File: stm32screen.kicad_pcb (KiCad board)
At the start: 4 copper layers, 49.8 x 49.8 mm, 43 parts, among them J1 SWD, J2 GC9A01, J3 Oil temp sensor, J4 pressure sensor, J5 USB_B_Micro, J6 EGT_sensor, SW1 SW_Push, SW2 SW_Push, U1 TS1117BCW-3.3, U2 STM32F407VETx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

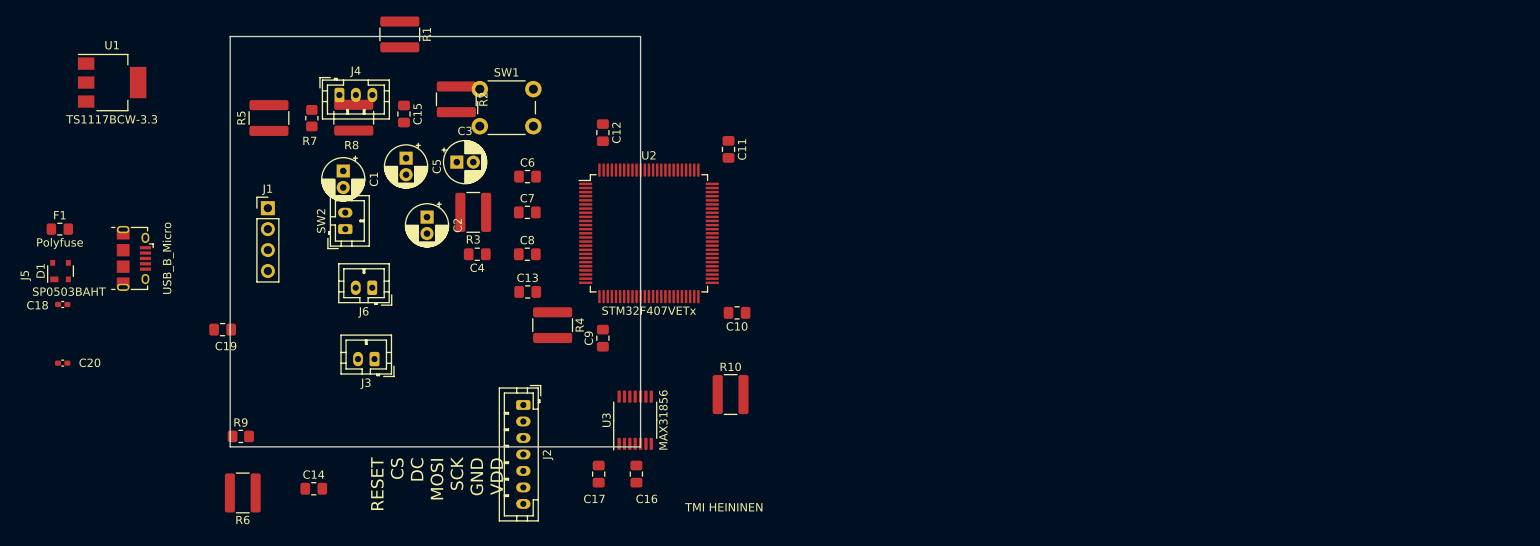
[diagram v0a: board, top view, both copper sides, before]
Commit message: Roughing out the PCB.
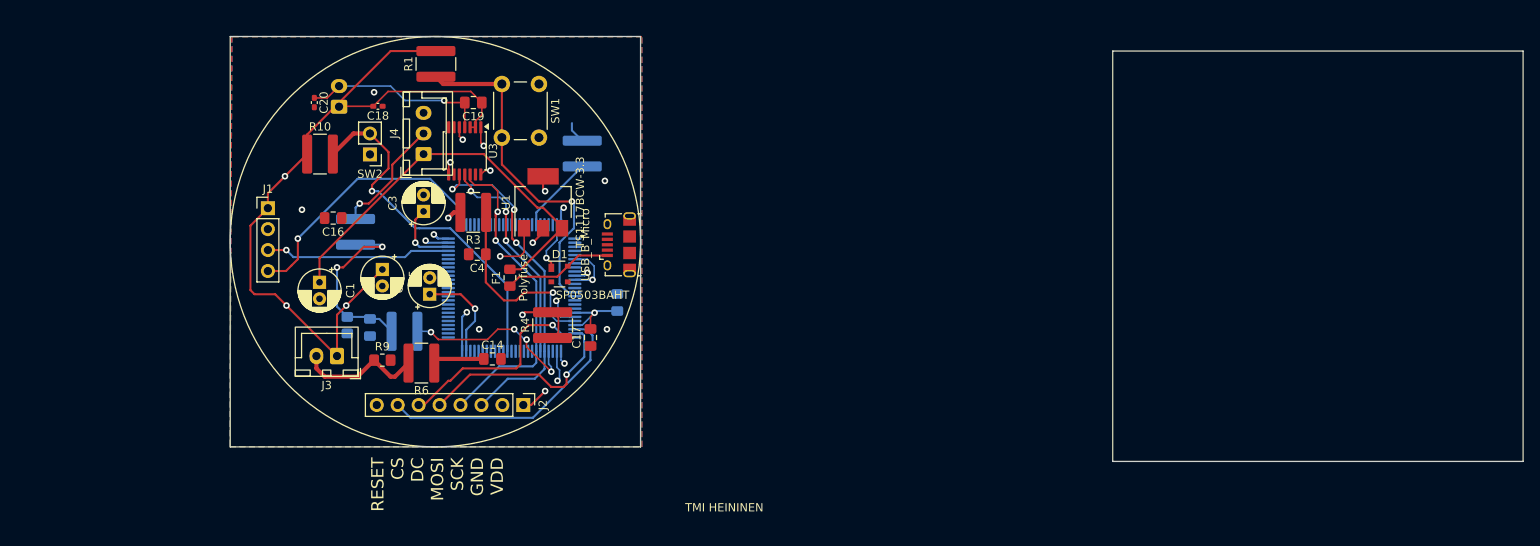
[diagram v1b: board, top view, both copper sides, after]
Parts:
- removed C10, C11, C12, C6, C7, C8, C9: 100nF, Capacitor_SMD:C_0805_2012Metric_Pad1.18x1.45mm_HandSolder
- C13, C15, R2, R5, R7, R8, U2: moved to B.Cu
- J2: footprint Connector_JST:JST_PH_B7B-PH-K_1x07_P2.00mm_Vertical -> Connector_PinHeader_2.54mm:PinHeader_1x08_P2.54mm_Vertical
- J3: footprint Connector_JST:JST_PH_B2B-PH-K_1x02_P2.00mm_Vertical -> Connector_JST:JST_XH_B2B-XH-A_1x02_P2.50mm_Vertical
- J4: footprint Connector_JST:JST_PH_B3B-PH-K_1x03_P2.00mm_Vertical -> Connector_JST:JST_XH_B3B-XH-A_1x03_P2.50mm_Vertical
- J6: footprint Connector_JST:JST_PH_B2B-PH-K_1x02_P2.00mm_Vertical -> Connector_JST:JST_XH_B2B-XH-A_1x02_P2.50mm_Vertical; moved to B.Cu
- SW2: footprint Connector_JST:JST_PH_B2B-PH-K_1x02_P2.00mm_Vertical -> Connector_PinHeader_2.54mm:PinHeader_1x02_P2.54mm_Vertical
- moved D1 60.5 mm to (138.0, 75.5), turned to 0 degrees
- moved J5 58.9 mm to (145.2, 72.0), turned to 90 degrees
- moved R10 57.7 mm to (108.9, 61.0)
- moved F1 54.9 mm to (132.0, 76.0), turned to 90 degrees
- moved U1 54.3 mm to (136.0, 66.8), turned to 90 degrees
- moved C16 48.1 mm to (110.5, 68.8), turned to 180 degrees
- moved C18 45.2 mm to (116.0, 55.2)
- moved C20 43.9 mm to (108.2, 54.8), turned to -90 degrees
- moved C19 41.0 mm to (127.5, 54.8)
- moved U3 38.7 mm to (126.5, 60.6), turned to -90 degrees
- moved R5 30.7 mm to (119.2, 82.5), turned to 180 degrees
- moved R6 26.8 mm to (121.2, 86.4)
- moved C14 26.8 mm to (129.9, 85.8)
- moved C15 26.2 mm to (115.0, 82.0)
- moved R7 25.5 mm to (112.2, 81.8)
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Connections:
- net /SCK renamed SCK
- net /SPI1_MOSI renamed SDI
- net Net-(U2-Pad31) renamed SDO
- C13 pad 2: Net-(C13-Pad2) -> VDD
- R4 pad 1: Net-(C13-Pad2) -> VDD
- U2 pad 22: Net-(C13-Pad2) -> VDD
- U2 pad 35: Net-(U2-Pad35) -> MAX_CS
- U2 pad 36: Net-(U2-Pad36) -> MAX-FAULT
- U2 pad 37: Net-(U2-Pad37) -> MAX_DRDY
- U3 pad 13: Net-(U2-Pad36) -> FAULT
- U3 pad 7: Net-(U2-Pad37) -> DRDY
- U3 pad 9: Net-(U2-Pad35) -> CS
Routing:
- net VDD: track 0.00 -> 114.6 mm, vias 0 -> 15
- net Vin: track 0.00 -> 49.8 mm
- net Net-(U2-PE8): track 0.00 -> 43.5 mm, vias 0 -> 1
- net SCK: track 0.00 -> 41.9 mm, vias 0 -> 3
- net NRST: track 0.00 -> 41.6 mm, vias 0 -> 1
- net SDI: track 0.00 -> 38.9 mm, vias 0 -> 2
- net /SWCLK: track 0.00 -> 33.0 mm, vias 0 -> 1
- net /RESET: track 0.00 -> 32.5 mm
- net GND: track 0.00 -> 30.6 mm, vias 0 -> 13
- net SDO: track 0.00 -> 26.9 mm, vias 0 -> 3
- net /CS: track 0.00 -> 25.8 mm, vias 0 -> 1
- net /D/C: track 0.00 -> 25.7 mm, vias 0 -> 1
- net Net-(U2-VREF+): track 0.00 -> 24.0 mm, vias 0 -> 1
- net Net-(J6-Pin_2): track 0.00 -> 22.7 mm, vias 0 -> 1
- net Net-(J6-Pin_1): track 0.00 -> 22.6 mm
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- added copper zone on B.Cu, net GND
- added copper zone on F.Cu, net GND
- added copper zone on In2.Cu, net GND
- added copper zone on In1.Cu, net VDD
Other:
- board size 49.8 x 49.8 mm -> 156.8 x 51.5 mm

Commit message: Routed rest of the unconnected pads
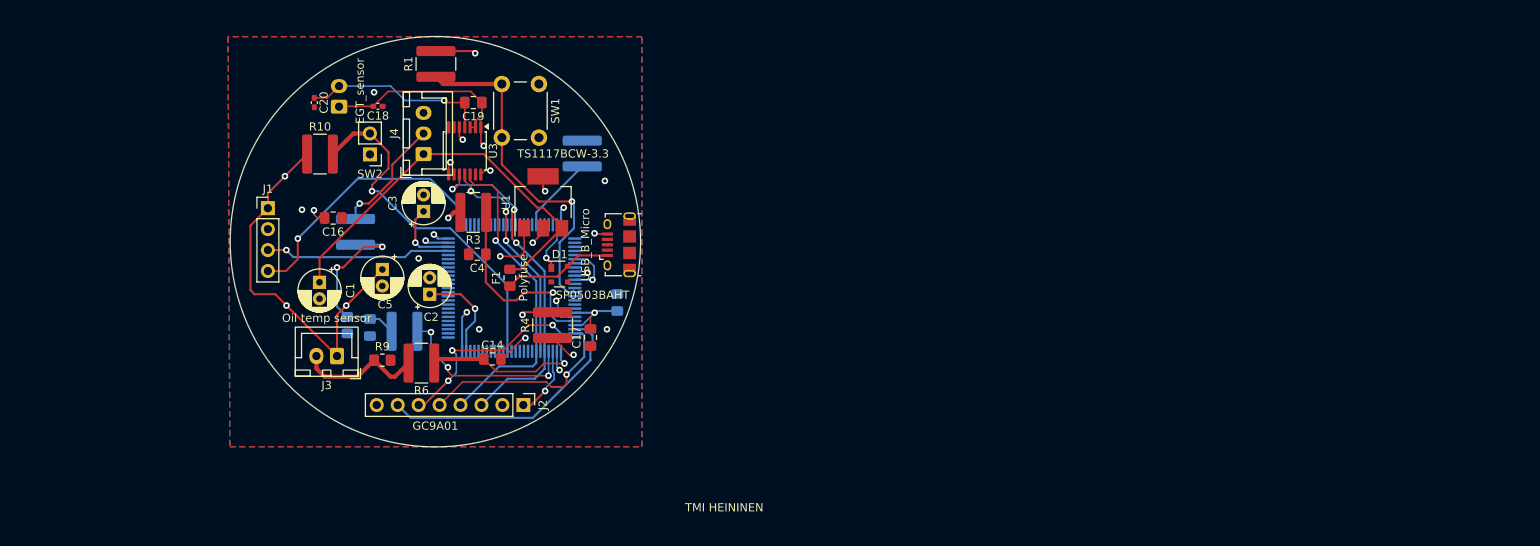
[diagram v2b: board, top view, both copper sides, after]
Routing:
- net Net-(U2-PA3): track 7.88 -> 18.7 mm
- net VDD: track 114.6 -> 104.3 mm, vias 15 -> 18
- net GND: track 30.6 -> 32.2 mm, vias 13 -> 16
- net /D/C: track 25.7 -> 25.0 mm
- net Net-(U2-PA4): track 22.5 -> 22.7 mm, vias 4 -> 3
- net /CS: track 25.8 -> 25.9 mm, vias 1 -> 3
- net SDI: vias 2 -> 1
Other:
- board size 156.8 x 51.5 mm -> 49.8 x 49.8 mm

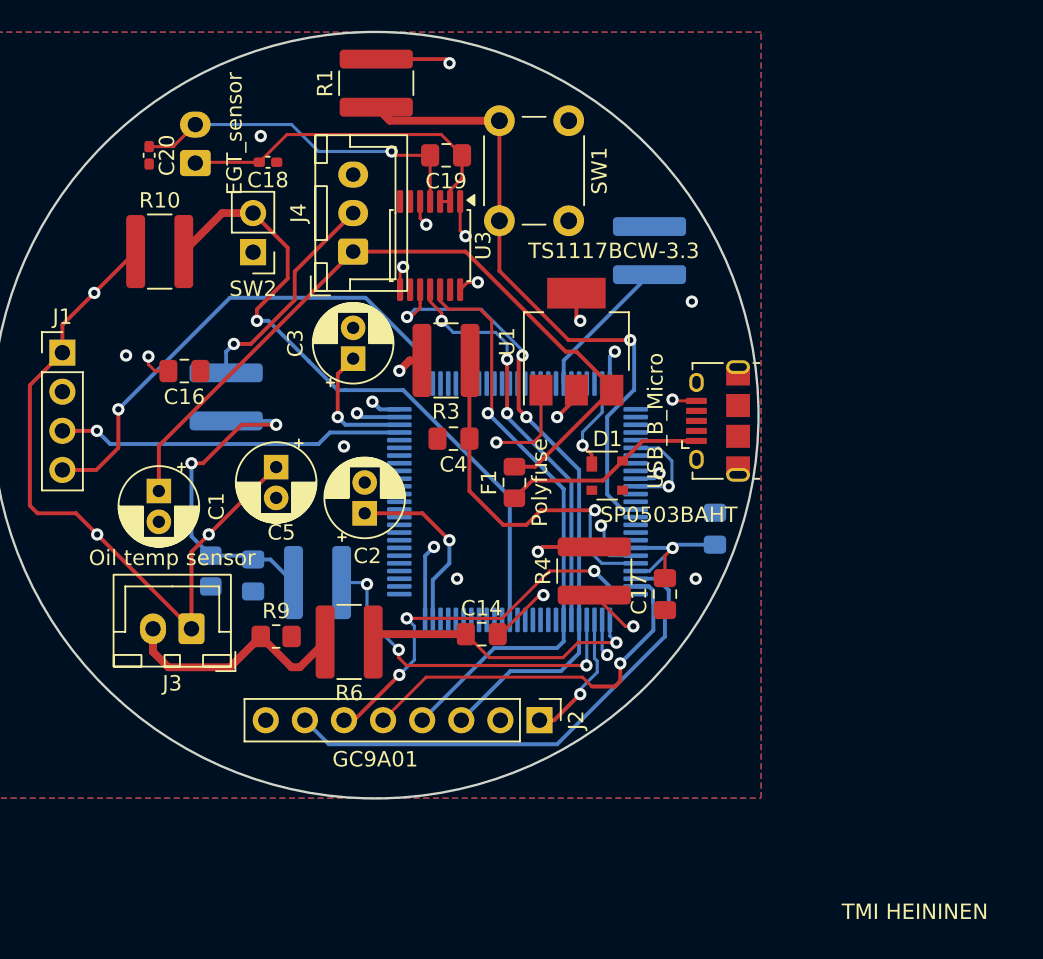
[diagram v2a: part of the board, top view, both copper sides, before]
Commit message: Added a status LED
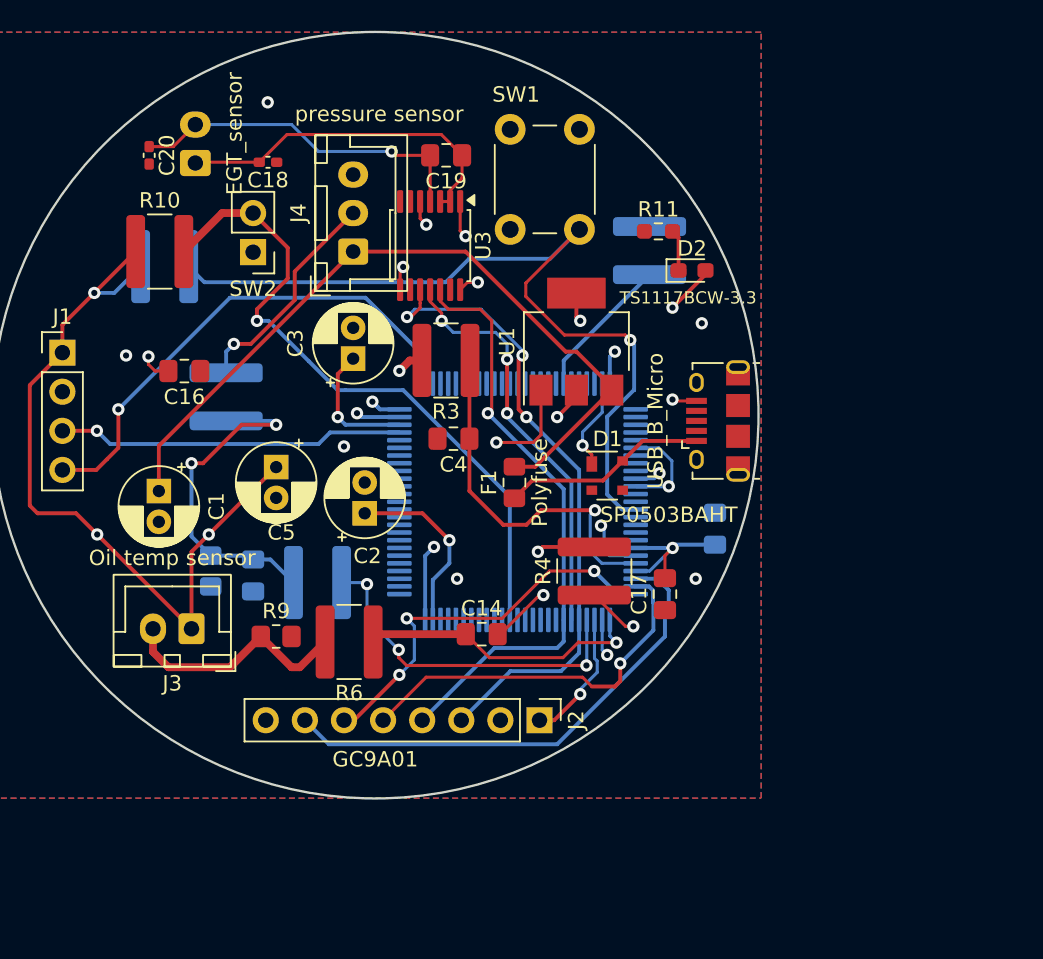
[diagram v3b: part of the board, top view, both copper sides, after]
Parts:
- added D2: LED, LED_SMD:LED_0603_1608Metric_Pad1.05x0.95mm_HandSolder, F.Cu at (143.5, 62.2)
- added R11: 68, Resistor_SMD:R_0603_1608Metric_Pad0.98x0.95mm_HandSolder, F.Cu at (141.3, 59.7)
- R1: moved to B.Cu
- moved R1 18.2 mm to (109.3, 62.0), turned to 180 degrees
- moved SW1 8.02 mm to (131.7, 59.6), turned to 90 degrees
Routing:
- net NRST: track 41.6 -> 54.1 mm
- net Net-(D2-K): track 0.00 -> 2.70 mm
- net VDD: track 104.3 -> 106.5 mm

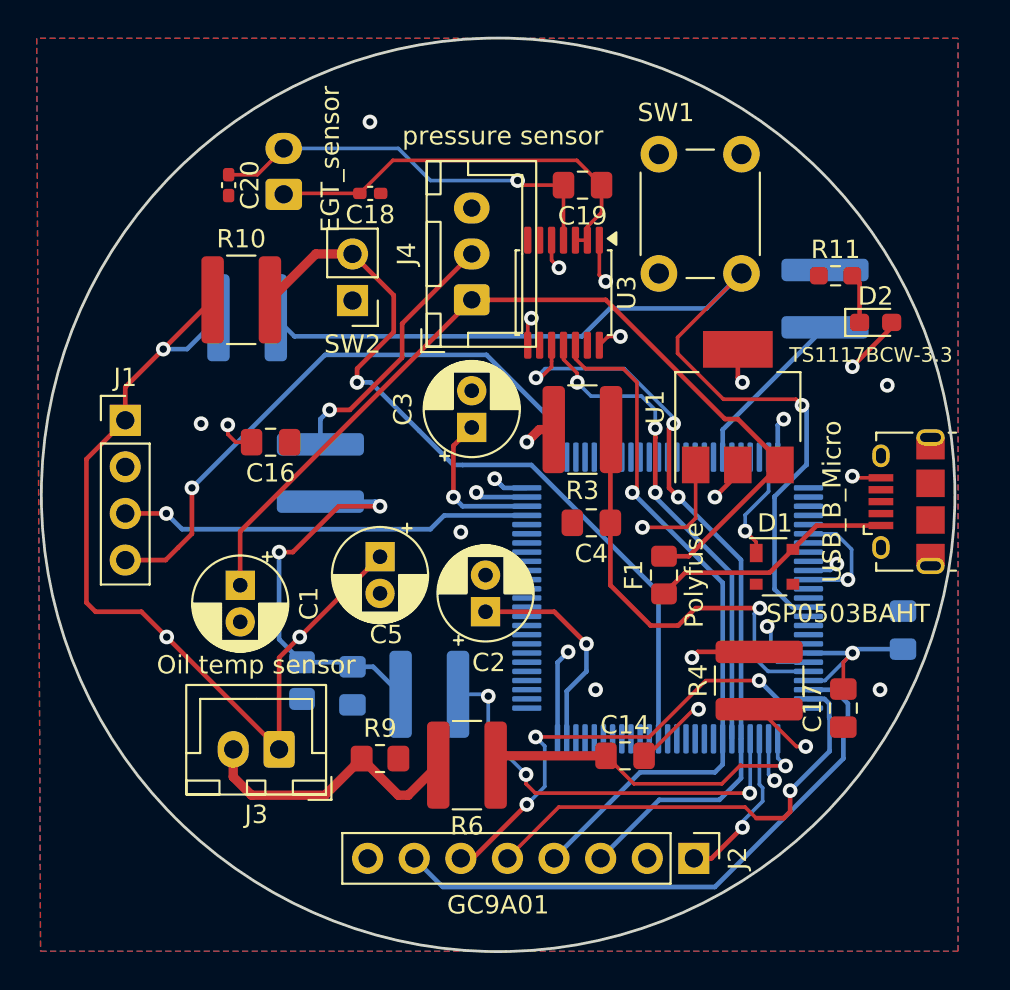
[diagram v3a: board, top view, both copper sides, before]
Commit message: Optimized PCB layout. Added images
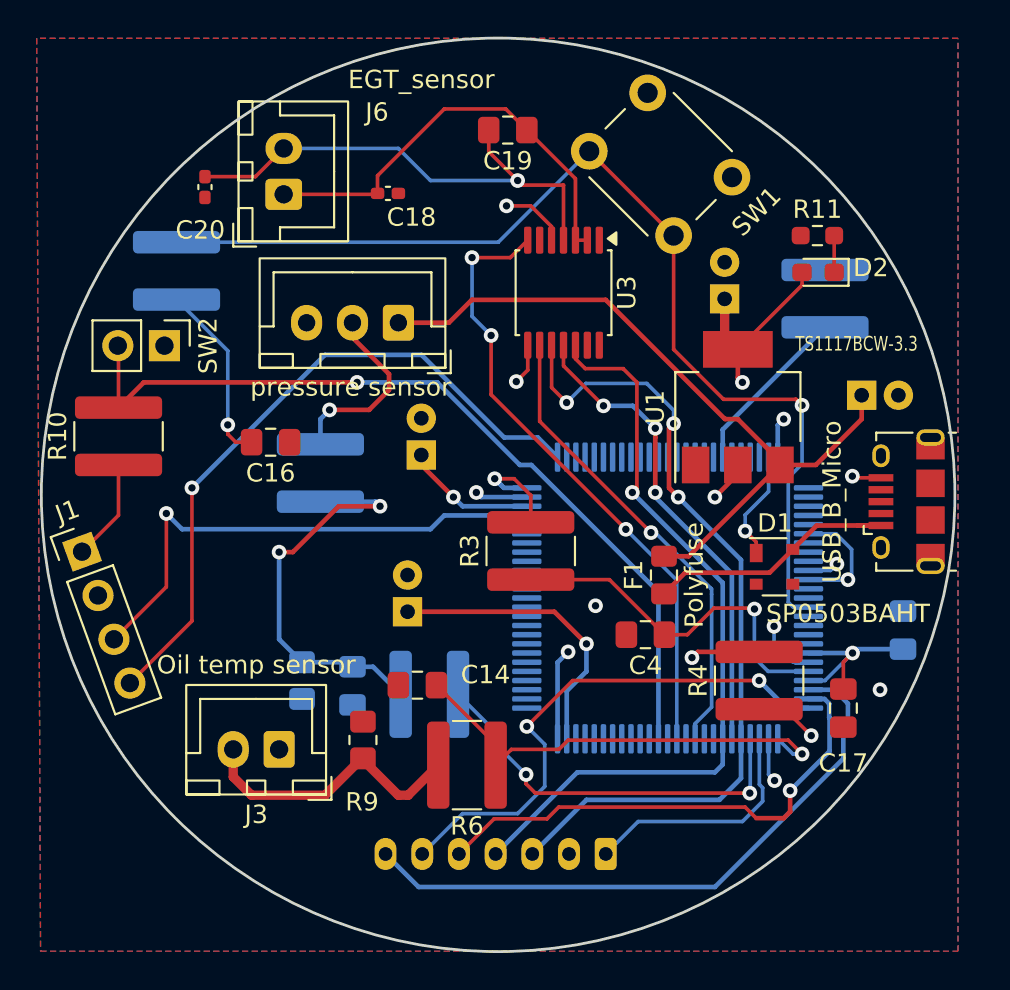
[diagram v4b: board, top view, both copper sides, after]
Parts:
- C1, C2, C3, C5: moved to B.Cu
- J2: footprint Connector_PinHeader_2.54mm:PinHeader_1x08_P2.54mm_Vertical -> Connector_JST:JST_PH_B7B-PH-K_1x07_P2.00mm_Vertical; moved to B.Cu
- J6: moved to F.Cu
- moved C1 35.4 mm to (142.8, 66.2), turned to 0 degrees
- moved C5 23.5 mm to (135.3, 60.9), turned to 90 degrees
- moved C14 12.0 mm to (118.5, 82.0), turned to 180 degrees
- moved SW2 10.5 mm to (104.8, 63.5), turned to -90 degrees
- moved R10 10.0 mm to (102.2, 68.4), turned to 90 degrees
- moved SW1 9.86 mm to (131.1, 49.7), turned to -45 degrees
- moved J1 7.54 mm to (100.3, 74.7), turned to 20 degrees
- moved R3 7.19 mm to (124.7, 74.7), turned to 90 degrees
- moved C4 6.77 mm to (131.0, 79.2)
- moved C19 5.06 mm to (123.5, 51.8)
- moved J2 4.81 mm to (128.8, 91.2), turned to 180 degrees
- moved R1 4.62 mm to (105.4, 59.4), turned to -90 degrees
- moved C2 4.25 mm to (118.0, 78.0)
- moved J4 4.19 mm to (117.5, 62.2), turned to 180 degrees
- moved D2 4.16 mm to (140.4, 59.5), turned to 180 degrees
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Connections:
- U3 pad 13: FAULT -> unconnected-(U3-~{FAULT}-Pad13)
- U3 pad 7: DRDY -> MAX_DRDY
- U3 pad 9: CS -> MAX_CS
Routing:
- net MAX_DRDY: track 0.00 -> 34.3 mm, vias 0 -> 3
- net MAX_CS: track 0.00 -> 25.9 mm, vias 0 -> 1
- net VDD: track 106.5 -> 85.1 mm, vias 18 -> 12
- net GND: track 32.2 -> 17.8 mm, vias 16 -> 8
- net Vin: track 49.8 -> 40.3 mm
- net Net-(U2-PA3): track 18.7 -> 24.9 mm
- net /SWDIO: track 22.5 -> 28.3 mm
- net Net-(J6-Pin_2): track 22.7 -> 27.4 mm
- net /SWCLK: track 33.0 -> 37.3 mm
- net Net-(U2-VCAP_1): track 11.8 -> 16.1 mm
- net Net-(J4-Pin_2): track 14.4 -> 10.3 mm
- net NRST: track 54.1 -> 57.8 mm
- net Net-(U2-VREF+): track 24.0 -> 20.4 mm
- net SCK: track 41.9 -> 45.2 mm
- net SDI: track 38.9 -> 42.0 mm
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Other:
- board text added: "TMI HEININEN 2026"
- board text removed: "TMI HEININEN"
